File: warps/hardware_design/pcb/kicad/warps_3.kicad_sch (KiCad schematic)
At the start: 54 parts

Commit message: warps caps + wm8731
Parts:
- C32, C37, C39, C43: footprint (none) -> plaits:PANASONIC_B
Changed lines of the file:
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@@
       (effects (font (size 1.778 1.5113)) (justify left bottom))
     )
-    (property "Footprint" "" (id 2) (at 195.58 109.22 0)
+    (property "Footprint" "plaits:PANASONIC_B" (id 2) (at 195.58 109.22 0)
       (effects (font (size 1.27 1.27)) hide)
     )
@@
       (effects (font (size 1.778 1.5113)) (justify left bottom))
     )
-    (property "Footprint" "" (id 2) (at 149.86 71.12 0)
+    (property "Footprint" "plaits:PANASONIC_B" (id 2) (at 149.86 71.12 0)
       (effects (font (size 1.27 1.27)) hide)
     )
@@
       (effects (font (size 1.778 1.5113)) (justify left bottom))
     )
-    (property "Footprint" "" (id 2) (at 149.86 109.22 0)
+    (property "Footprint" "plaits:PANASONIC_B" (id 2) (at 149.86 109.22 0)
       (effects (font (size 1.27 1.27)) hide)
     )
@@
       (effects (font (size 1.778 1.5113)) (justify left bottom))
     )
-    (property "Footprint" "" (id 2) (at 195.58 71.12 0)
-      (effects (font (size 1.27 1.27)) hide)
-    )
+    (property "Footprint" "plaits:PANASONIC_B" (id 2) (at 195.58 71.12 0)
+      (effects (font (size 1.27 1.27)) hide)
+    )

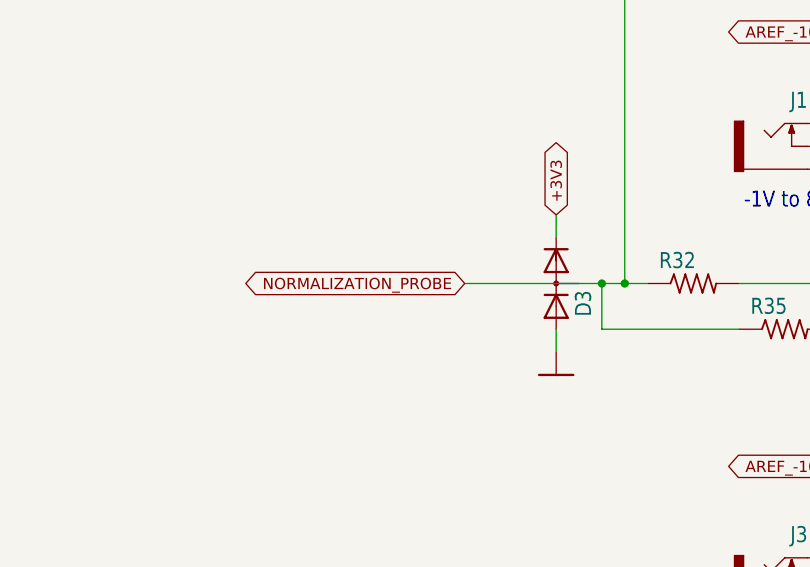
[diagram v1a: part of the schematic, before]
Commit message: warps cleanup tracks and vias
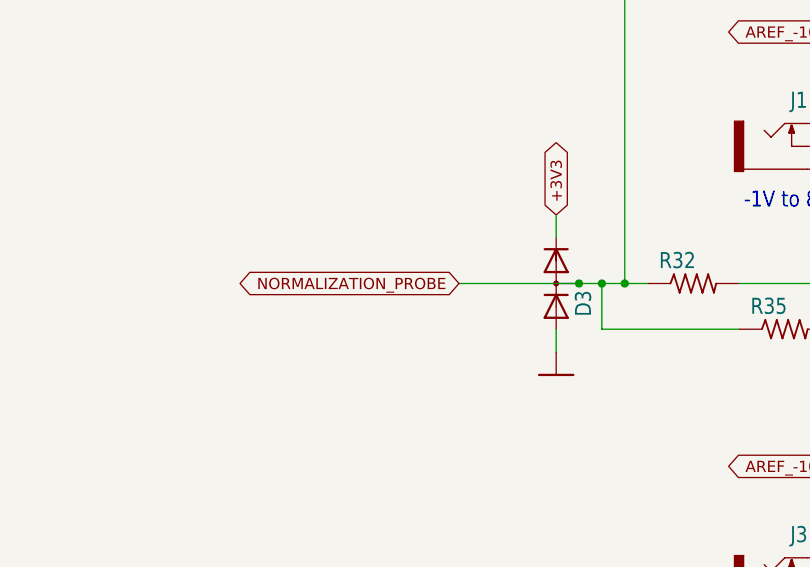
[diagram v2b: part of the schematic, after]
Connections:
- net NORMALIZATION_PROBE: now also D3.3 (AC)
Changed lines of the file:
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@@
   (junction (at 152.4 228.6) (diameter 0) (color 0 0 0 0)
   )
+  (junction (at 88.9 195.58) (diameter 0) (color 0 0 0 0)
+  )
   (junction (at 203.2 71.12) (diameter 0) (color 0 0 0 0)
   )
@@
     (stroke (width 0) (type default) (color 0 0 0 0))
   )
+  (wire (pts (xy 88.9 195.58) (xy 91.44 195.58))
+    (stroke (width 0) (type default) (color 0 0 0 0))
+  )
   (wire (pts (xy 121.92 132.08) (xy 121.92 134.62))
     (stroke (width 0) (type default) (color 0 0 0 0))
@@
     (stroke (width 0) (type default) (color 0 0 0 0))
   )
-  (wire (pts (xy 76.2 195.58) (xy 91.44 195.58))
+  (wire (pts (xy 75.565 195.58) (xy 88.9 195.58))
     (stroke (width 0) (type default) (color 0 0 0 0))
   )
@@
     )
   )
-  (global_label "NORMALIZATION_PROBE" (shape bidirectional) (at 76.2 195.58 180) (fields_autoplaced)
+  (global_label "NORMALIZATION_PROBE" (shape bidirectional) (at 75.565 195.58 180) (fields_autoplaced)
     (effects (font (size 1.2446 1.2446)) (justify right))
-    (property "Intersheet References" "${INTERSHEET_REFS}" (id 0) (at -259.08 121.92 0)
+    (property "Intersheet References" "${INTERSHEET_REFS}" (id 0) (at -259.715 121.92 0)
       (effects (font (size 1.27 1.27)) hide)
     )

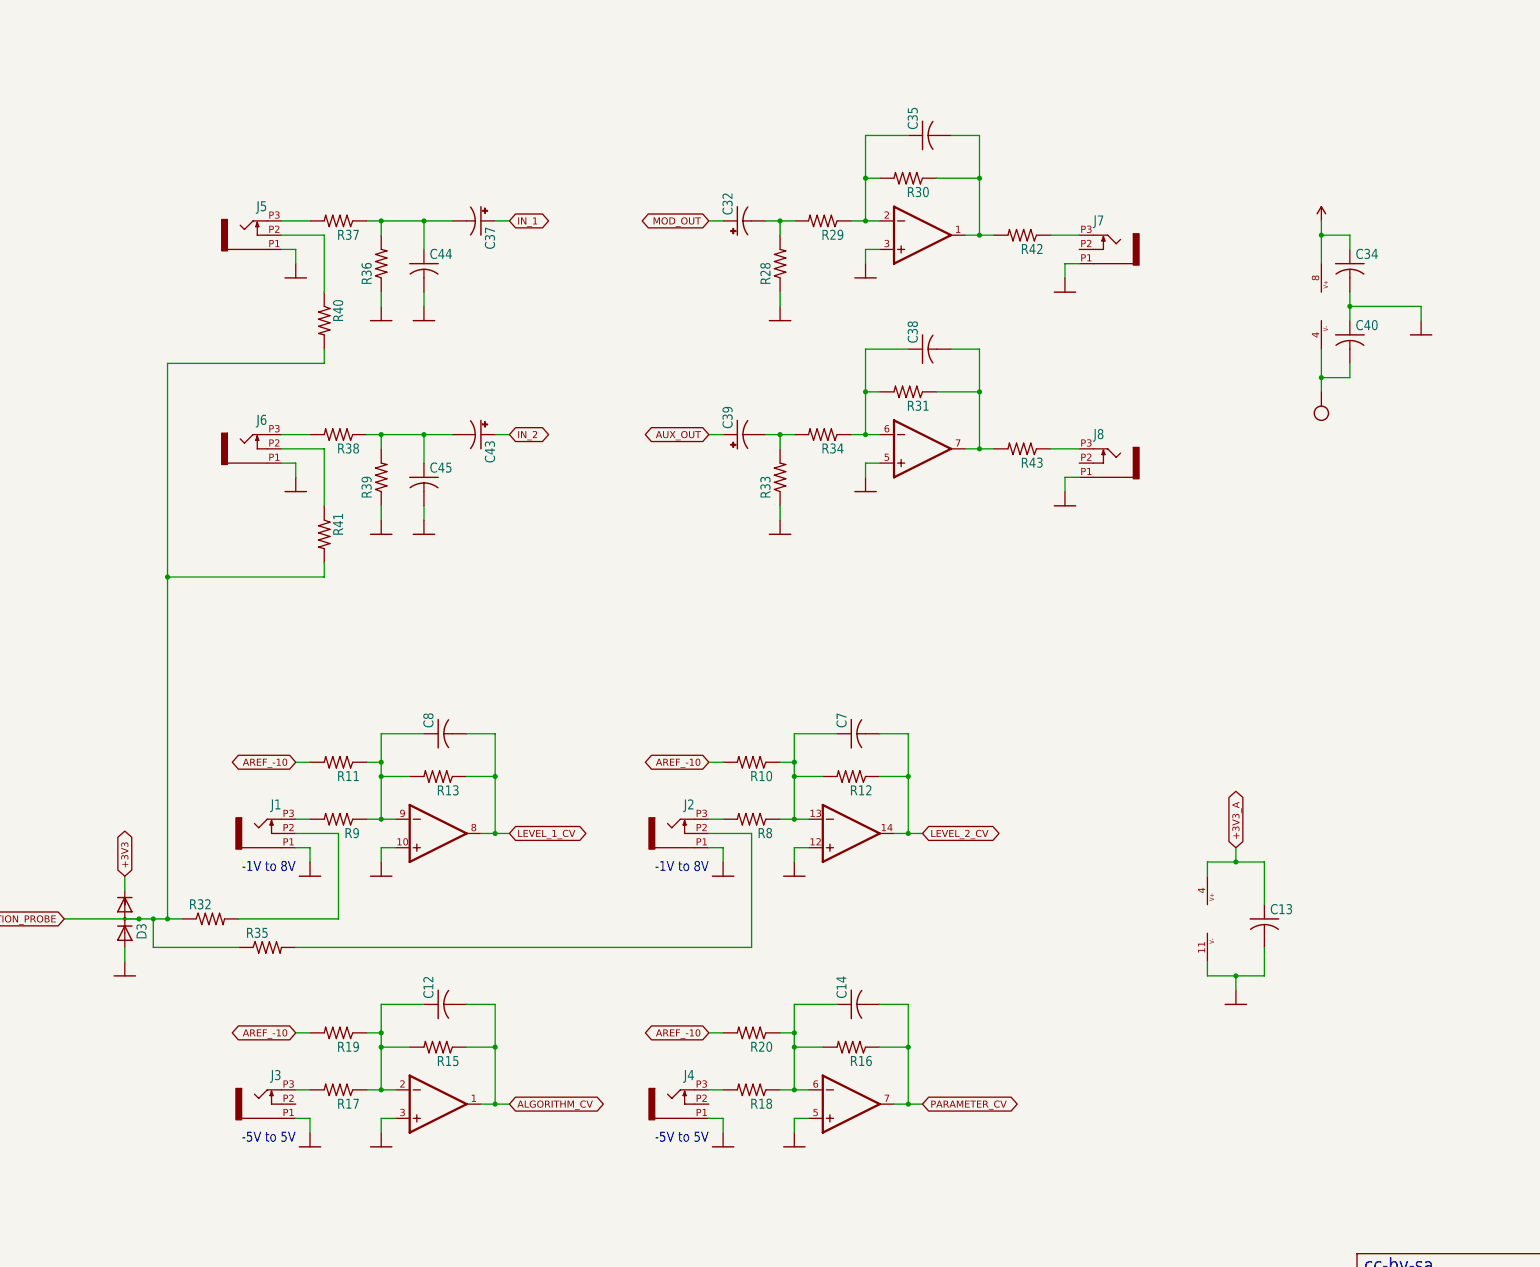
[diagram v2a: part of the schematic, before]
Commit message: warps SMD boot/reset buttons
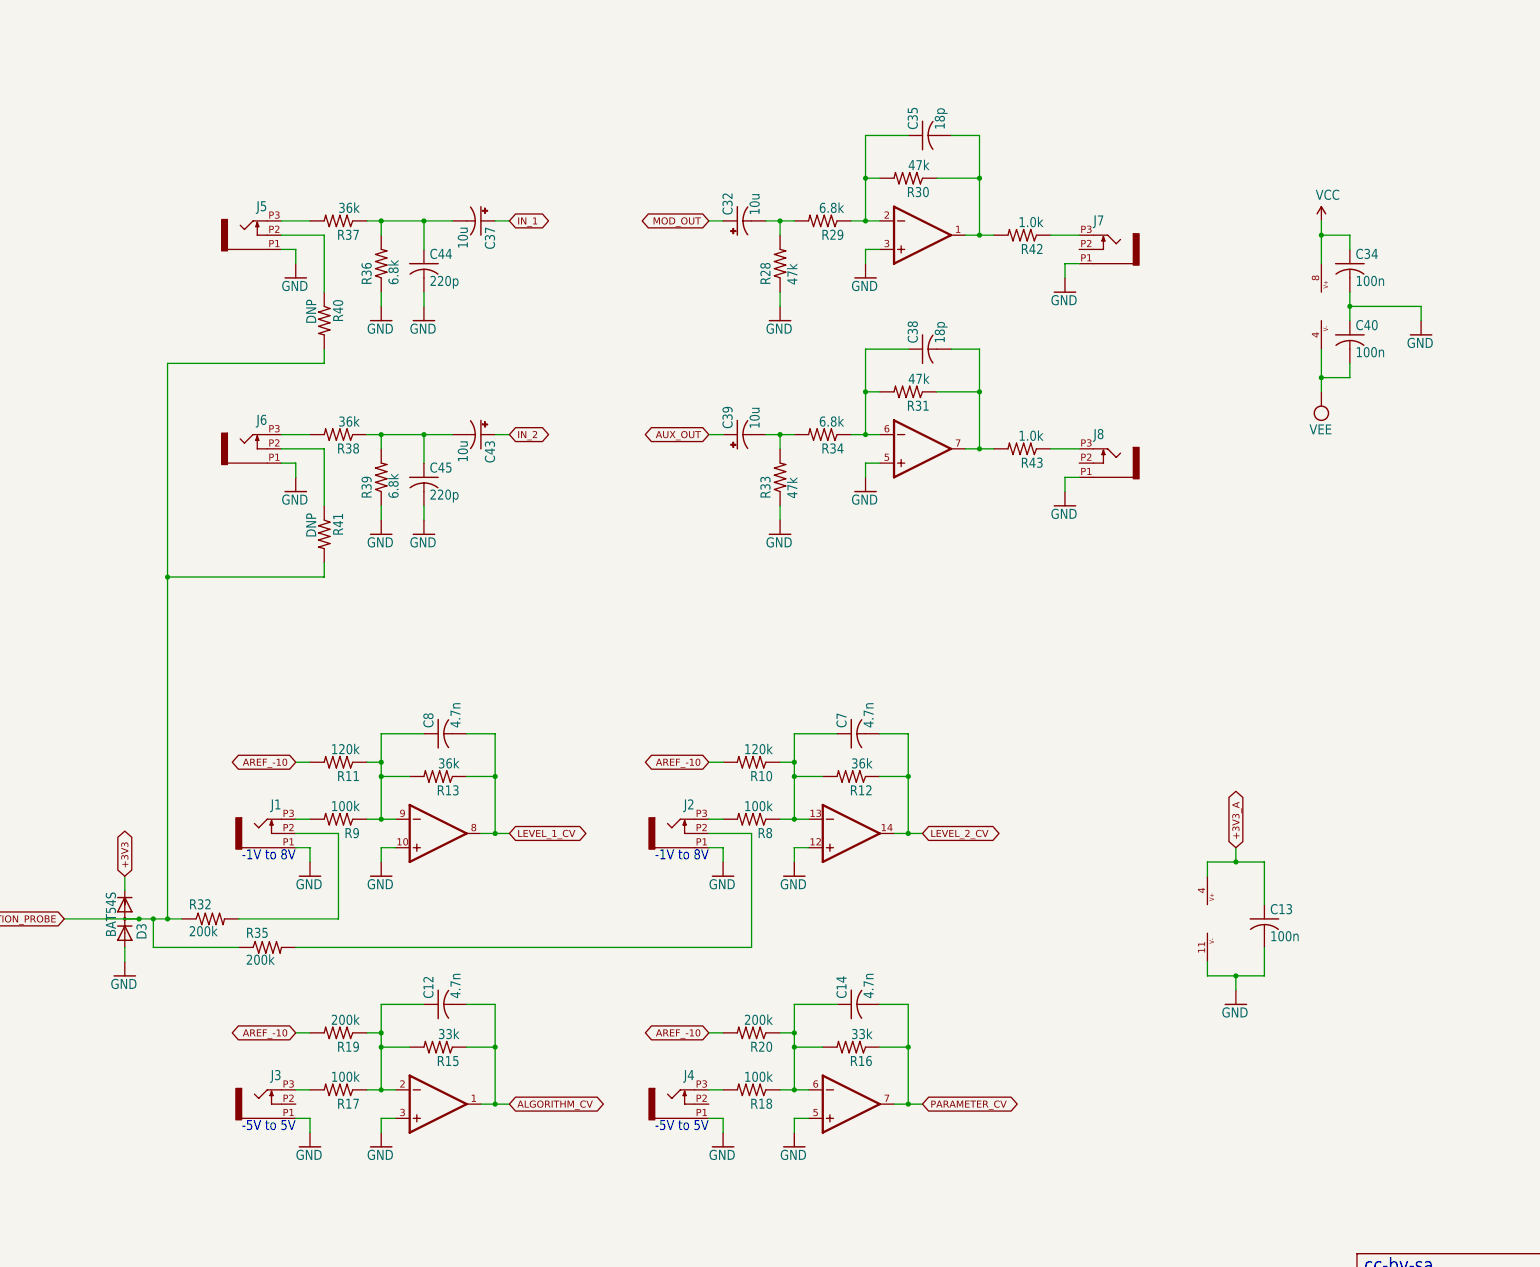
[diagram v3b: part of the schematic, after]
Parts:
- C12, C14, C7, C8: value (none) -> 4.7n; footprint (none) -> warps:C0603
- C13, C34, C40: value (none) -> 100n; footprint (none) -> warps:C0603
- C32, C37, C39, C43: value (none) -> 10u
- C35, C38: value (none) -> 18p; footprint (none) -> warps:C0603
- C44, C45: value (none) -> 220p; footprint (none) -> warps:C0603
- D3: value (none) -> BAT54S; footprint (none) -> warps:SOT23
- IC3: value (none) -> MCP6004; footprint (none) -> warps:SO14
- IC6: value (none) -> TL072; footprint (none) -> warps:SO08
- J1, J2, J3, J4, J5, J6, J7, J8: value (none) -> PJ301_THONKICONN6; footprint (none) -> warps:WQP_PJ_301M6
- R10, R11: value (none) -> 120k; footprint (none) -> warps:R0603
- R12, R13, R37, R38: value (none) -> 36k; footprint (none) -> warps:R0603
- R15, R16: value (none) -> 33k; footprint (none) -> warps:R0603
- R17, R18, R8, R9: value (none) -> 100k; footprint (none) -> warps:R0603
- R19, R20, R32, R35: value (none) -> 200k; footprint (none) -> warps:R0603
- R28, R30, R31, R33: value (none) -> 47k; footprint (none) -> warps:R0603
- R29, R34, R36, R39: value (none) -> 6.8k; footprint (none) -> warps:R0603
- R40, R41: value (none) -> DNP; footprint (none) -> warps:R0603
- R42, R43: value (none) -> 1.0k; footprint (none) -> warps:R0603
